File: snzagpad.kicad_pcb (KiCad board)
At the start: 2 copper layers, 74.8 x 99.8 mm, 93 parts, among them J1 USB_C, J2 SWD, SW1 ?, SW10 ?, SW11 ?, SW12 ?, SW13 ?, SW14 ?, SW15 ?, SW16 ?, SW17 ?, SW18 ?, SW19 ?, SW2 ?, SW20 ?, SW21 ?, SW22 ?, SW23 ?, SW24 Boot, SW3 ?, SW4 ?, SW5 ?, SW6 ?, SW7 ?, SW8 ?, SW9 ?, U1 XC6206, U2 RP2040, U3 SRV05-4, U4 W25Q128JVS, Y1 12MHz

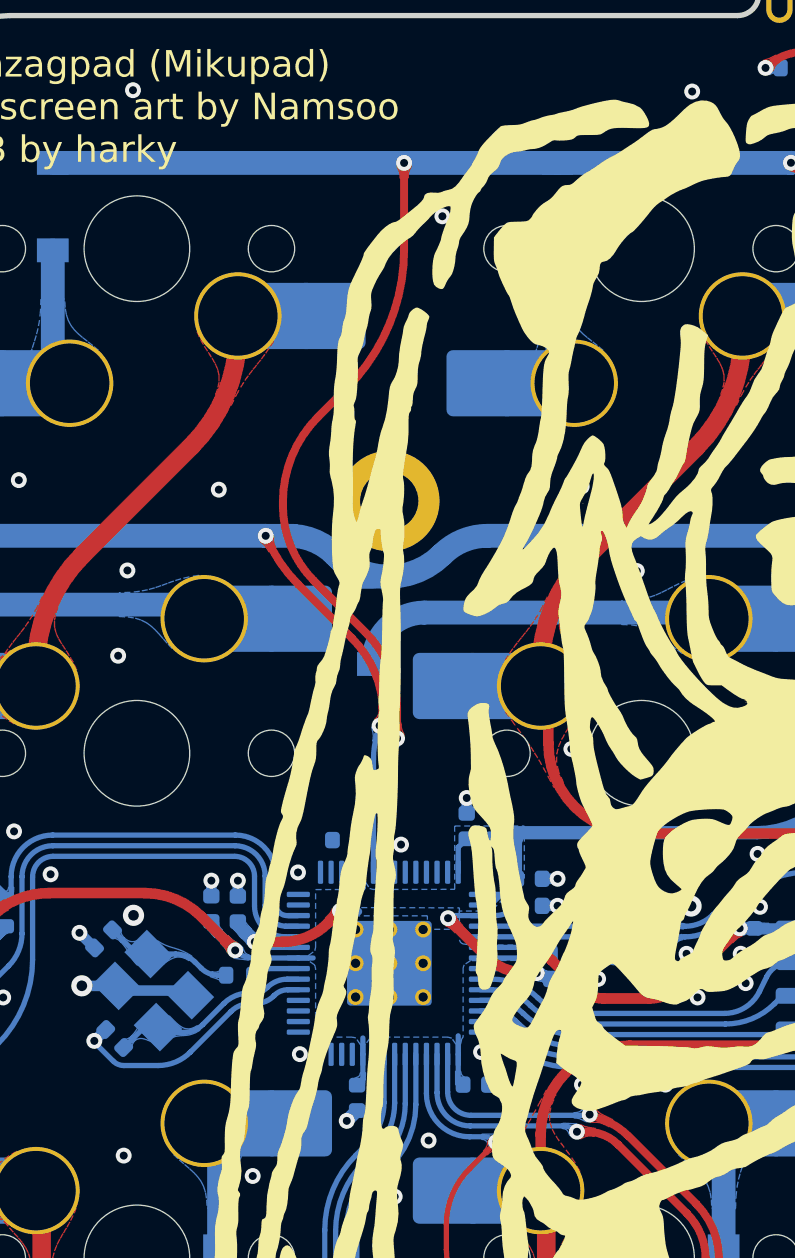
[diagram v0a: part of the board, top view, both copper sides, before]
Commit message: Added GPIO breakout
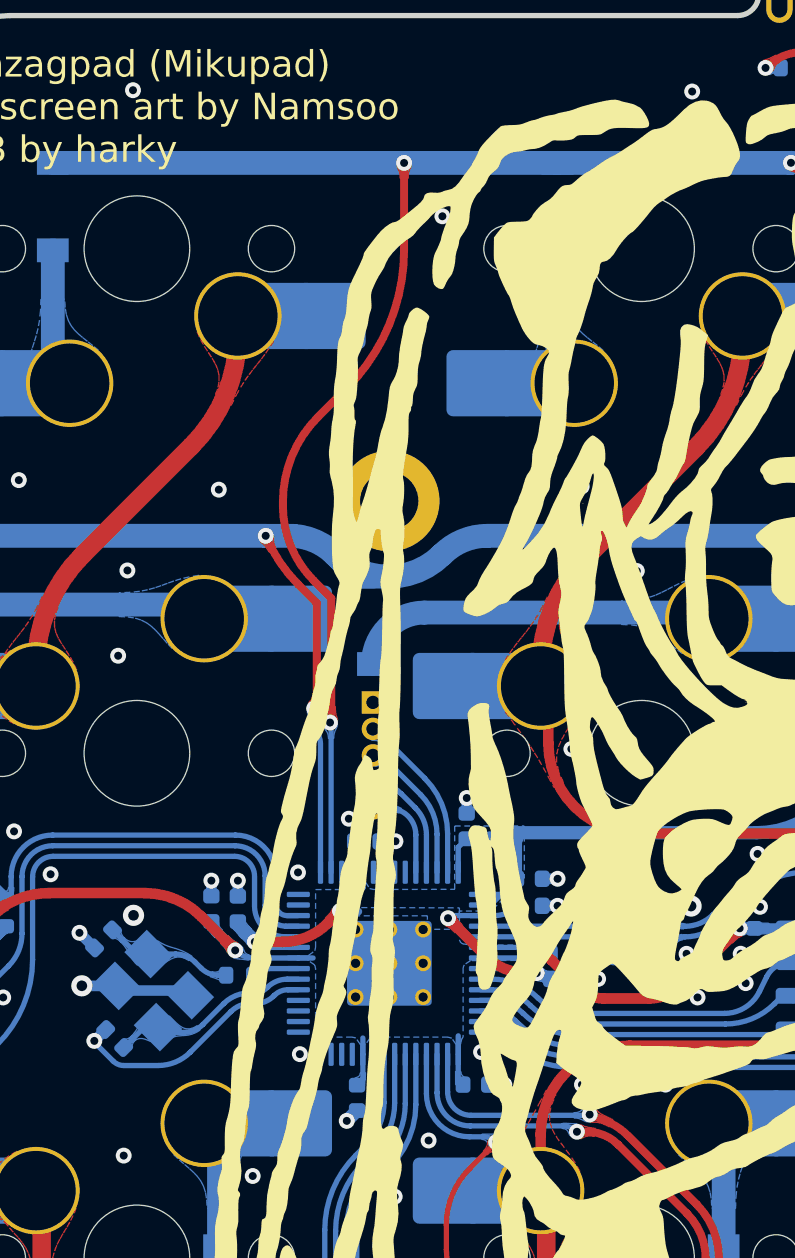
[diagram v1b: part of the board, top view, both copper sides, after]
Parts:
- added J3: Conn_01x05, Connector_PinHeader_1.00mm:PinHeader_1x05_P1.00mm_Vertical, F.Cu at (51.0, 79.0)
- moved C17 0.83 mm to (50.8, 84.3), turned to 0 degrees
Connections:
- U2 pad 29: unconnected-(U2-Pad29) -> ROW1
- U2 pad 30: unconnected-(U2-Pad30) -> ROW0
- U2 pad 34: ROW1 -> unconnected-(U2-Pad34)
- U2 pad 35: ROW0 -> unconnected-(U2-Pad35)
- U2 pad 38: unconnected-(U2-Pad38) -> GP26
- U2 pad 39: unconnected-(U2-Pad39) -> GP27
- U2 pad 40: unconnected-(U2-Pad40) -> GP28
- U2 pad 41: unconnected-(U2-Pad41) -> GP29
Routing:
- net GP29: track 0.00 -> 6.49 mm
- net GP28: track 0.00 -> 5.50 mm
- net GP27: track 0.00 -> 4.47 mm
- net GP26: track 0.00 -> 3.56 mm
- net ROW0: track 86.9 -> 86.0 mm
- net ROW1: track 90.2 -> 89.4 mm
- net GND: vias 123 -> 124
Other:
- board text added: "GP29 GP26"

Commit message: Minor change, updated manufacturing files, added step file
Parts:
- moved C11 0.73 mm to (54.4, 94.1), turned to -90 degrees
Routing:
- net ROW2: track 57.6 -> 59.4 mm
- net ROW3: track 82.3 -> 83.1 mm
- net ROW4: track 110.5 -> 111.3 mm
- net GND: track 25.6 -> 26.3 mm, vias 124 -> 125
